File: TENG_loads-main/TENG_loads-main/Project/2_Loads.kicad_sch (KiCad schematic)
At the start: 7 parts, among them IC4 74HC238D,653, IC6 TBD62083AFG, IC7 TBD62083AFG

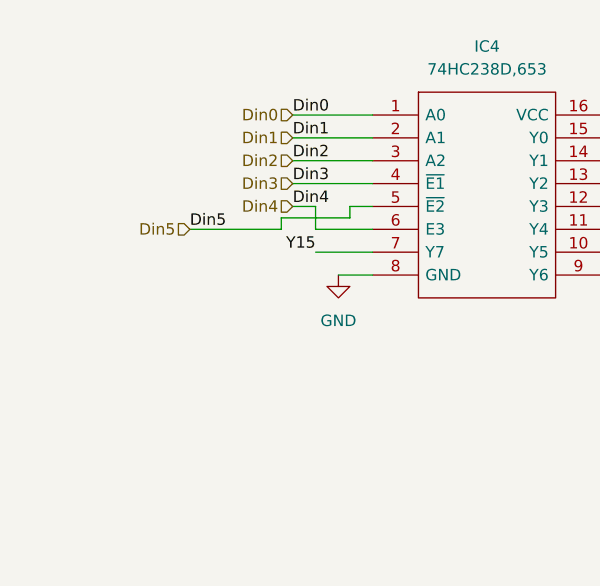
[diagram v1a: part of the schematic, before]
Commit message: Pull Down Resistor and reconnect
Introduced the pull down resistors and reconnect all the unconnected tracks. The position of some items has changed to fit the new components.
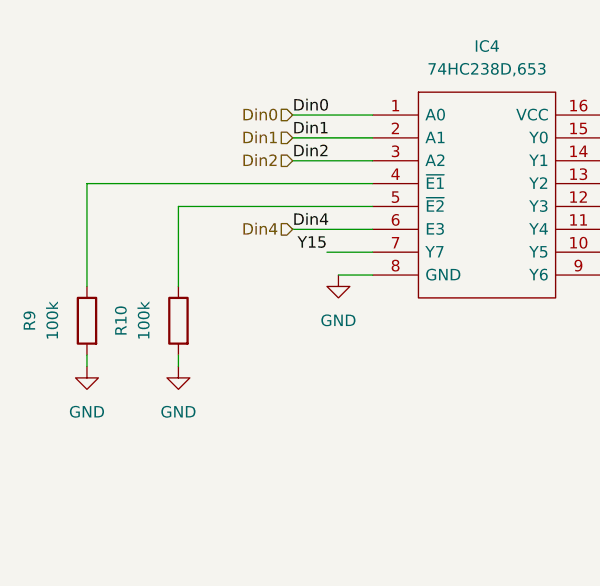
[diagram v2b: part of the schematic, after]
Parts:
- added R10, R9: 100k, Resistor_SMD:R_0805_2012Metric, symbol Device:R
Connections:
- net GND: now also R10.2, R9.2
- net Din3: no longer names the net of IC4.4 (~{E1})
- net Din3: now also R9.1
- net Din5: no longer names the net of IC4.5 (~{E2})
- net Din5: now also R10.1
